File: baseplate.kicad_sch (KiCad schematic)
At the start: 8 parts, among them U1 STM32L011F4Ux, U1 TLE5009E1000FUMA1, U15 DF52-4S-0.8H(21)

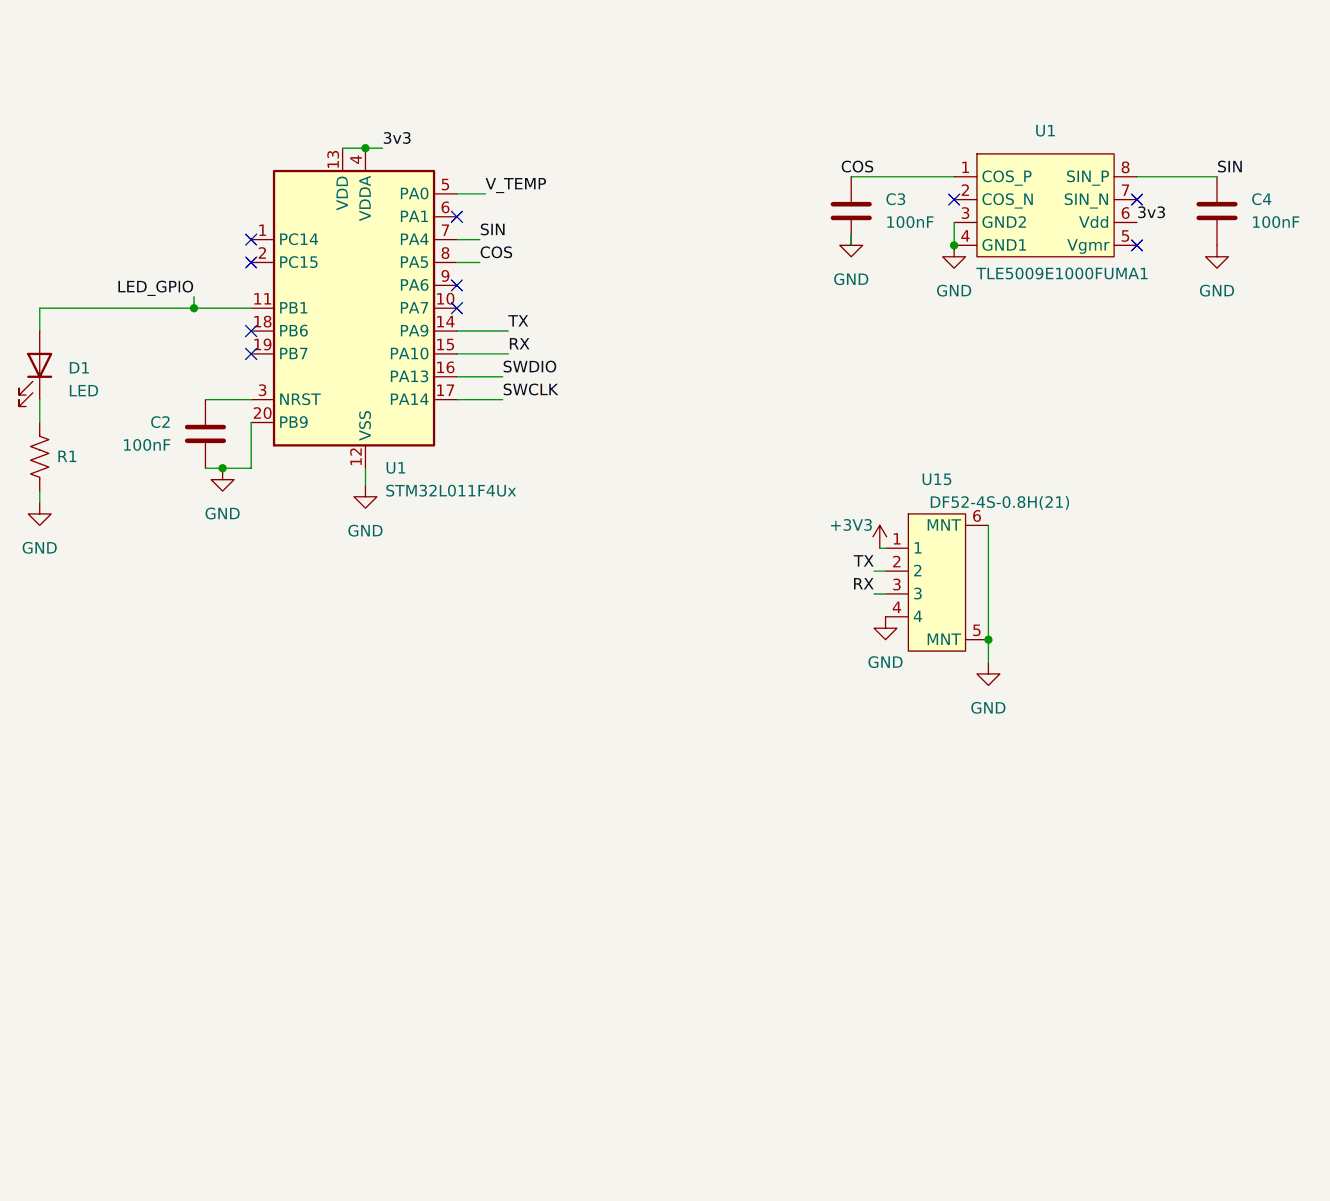
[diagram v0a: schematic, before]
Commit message: dxfs copied over, baseplate pcb fully designed, more lib management
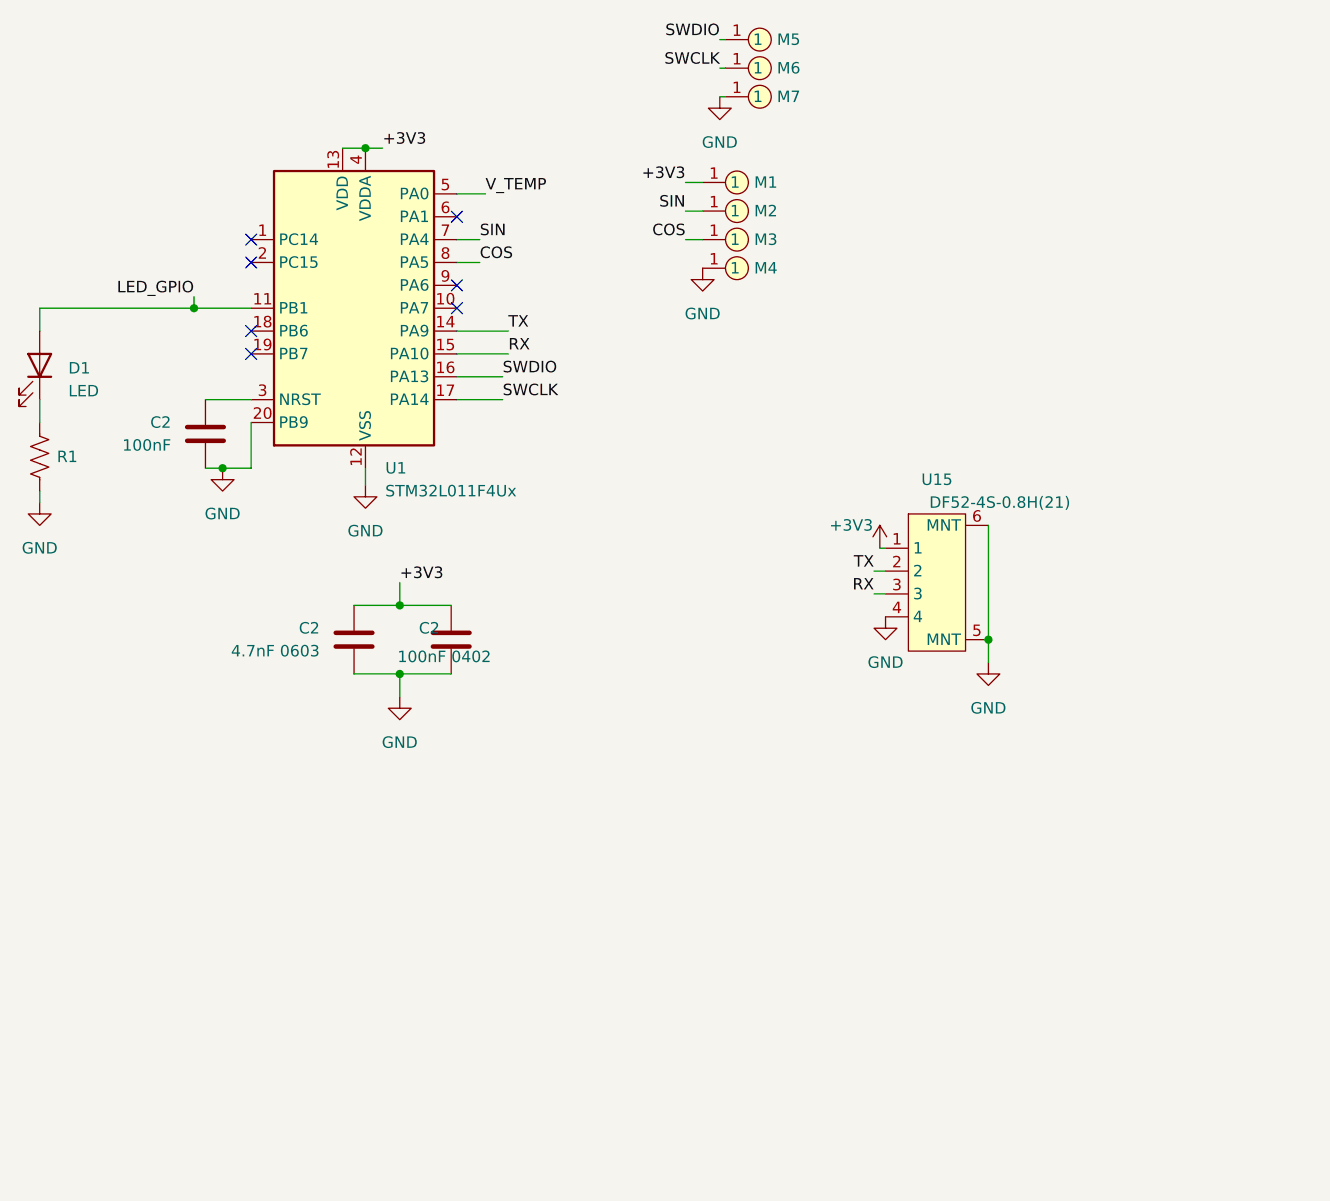
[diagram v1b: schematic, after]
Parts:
- removed C3, C4: 100nF, adapter-encoder:C_0402_1005Metric, symbol adapter-encoder:Capacitor
- removed U1: TLE5009E1000FUMA1, adapter-encoder:SOIC8-TLE5009, symbol adapter-encoder:TLE5009E1000FUMA1
- added C2: 4.7nF 0603, adapter-encoder:C_0603_1608Metric, symbol adapter-encoder:Capacitor
- added C2: 100nF 0402, adapter-encoder:C_0402_1005Metric, symbol adapter-encoder:Capacitor
- added M1, M4: THRU_HOLE_PAD, adapter-encoder:dogbone_slot, symbol adapter-encoder:THRU_HOLE_PAD
- added M2, M3: THRU_HOLE_PAD, adapter-encoder:dogbone_pad, symbol adapter-encoder:THRU_HOLE_PAD
- added M5, M6, M7: THRU_HOLE_PAD, foc-pcb-library:PAD-BREADBOARD, symbol adapter-encoder:THRU_HOLE_PAD
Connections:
- net 3v3 is gone; now on net +3V3: U1.13 (VDD), U1.4 (VDDA)
- net +3V3: now also C2.1, C2.1, M1.1
- net COS: now also M3.1
- net GND: now also C2.2, C2.2, M4.1, M7.1
- net SIN: now also M2.1
- net SWCLK: now also M6.1
- net SWDIO: now also M5.1
- no-connect marks 10 -> 7

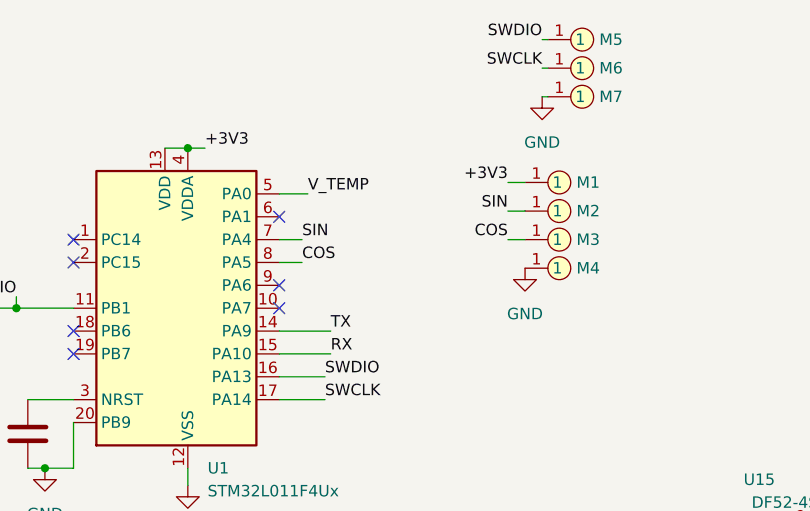
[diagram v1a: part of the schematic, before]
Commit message: net labelling, silkscreen, boards finished
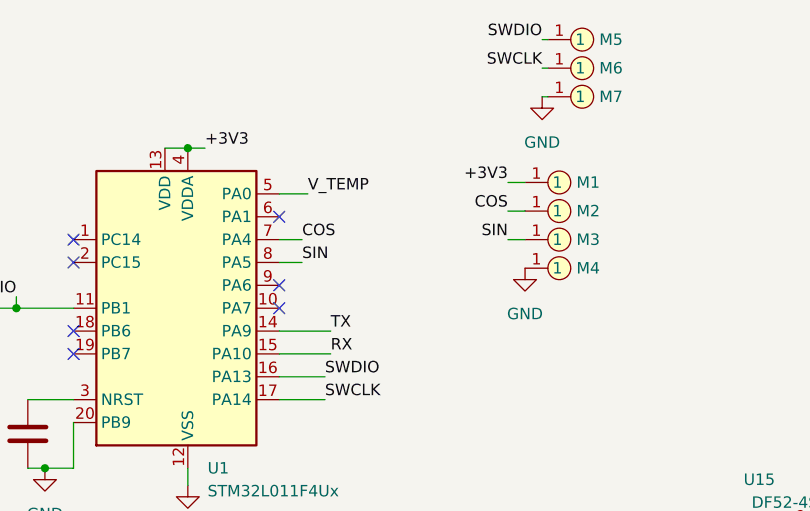
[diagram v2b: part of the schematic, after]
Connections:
- net COS: now also M2.1, U1.7 (PA4); no longer M3.1, U1.8 (PA5)
- net SIN: now also M3.1, U1.8 (PA5); no longer M2.1, U1.7 (PA4)
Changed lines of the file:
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@@
     (effects (font (size 1.27 1.27)) (justify right bottom))
   )
-  (label "COS" (at 106.68 37.465 180) (fields_autoplaced)
+  (label "SIN" (at 106.68 37.465 180) (fields_autoplaced)
     (effects (font (size 1.27 1.27)) (justify right bottom))
   )
@@
     (effects (font (size 1.27 1.27)) (justify left bottom))
   )
+  (label "COS" (at 83.82 37.465 0) (fields_autoplaced)
+    (effects (font (size 1.27 1.27)) (justify left bottom))
+  )
   (label "+3V3" (at 74.93 75.565 0) (fields_autoplaced)
     (effects (font (size 1.27 1.27)) (justify left bottom))
   )
-  (label "SIN" (at 83.82 37.465 0) (fields_autoplaced)
-    (effects (font (size 1.27 1.27)) (justify left bottom))
+  (label "COS" (at 106.68 34.29 180) (fields_autoplaced)
+    (effects (font (size 1.27 1.27)) (justify right bottom))
   )
-  (label "COS" (at 83.82 40.005 0) (fields_autoplaced)
+  (label "SIN" (at 83.82 40.005 0) (fields_autoplaced)
     (effects (font (size 1.27 1.27)) (justify left bottom))
   )
@@
     (effects (font (size 1.27 1.27)) (justify right bottom))
   )
-  (label "SIN" (at 106.68 34.29 180) (fields_autoplaced)
-    (effects (font (size 1.27 1.27)) (justify right bottom))
-  )

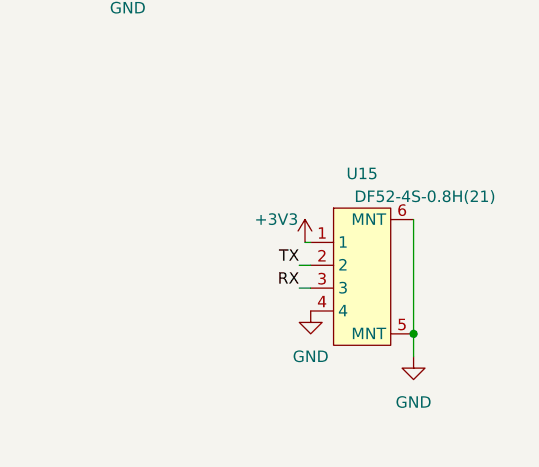
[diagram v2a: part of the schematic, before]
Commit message: step files from freecad, put the connector on the baseplate on the bottom of the baseplate
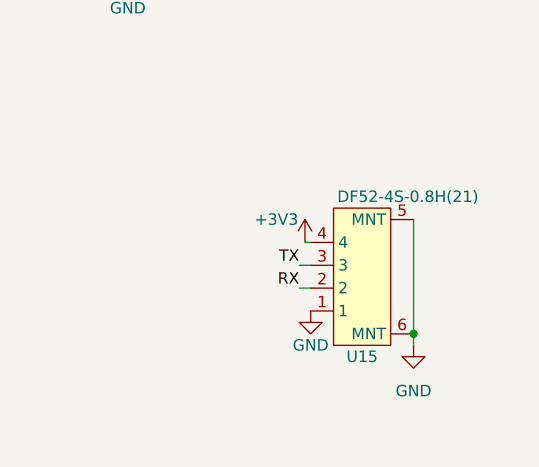
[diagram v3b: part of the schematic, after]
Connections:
- net +3V3: now also U15.4; no longer U15.1
- net GND: now also U15.1; no longer U15.4
- net RX: now also U15.2; no longer U15.3
- net TX: now also U15.3; no longer U15.2

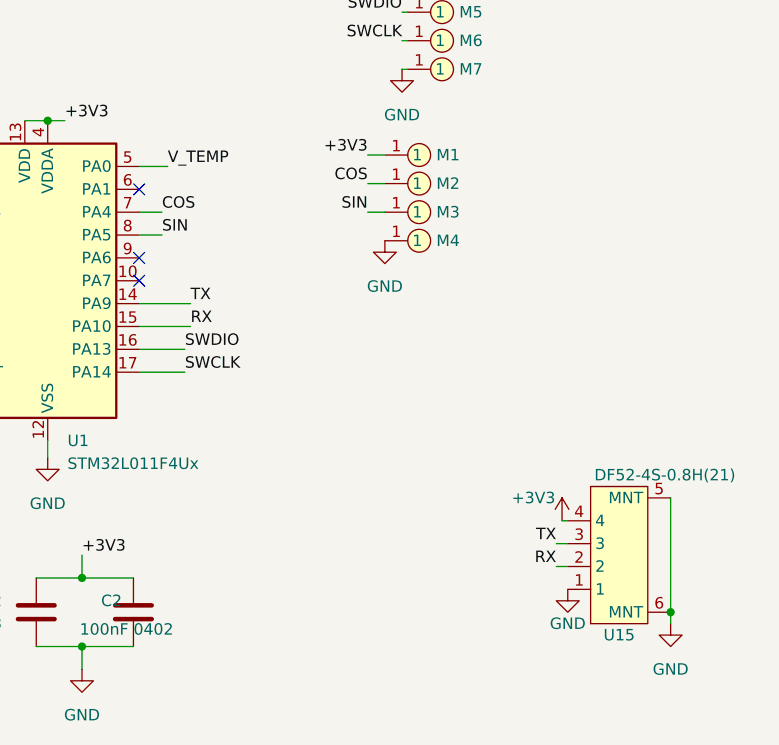
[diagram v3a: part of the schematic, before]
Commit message: reverted baseplate back to all on top, designed to flip over, and solder from the component side. dogbone bottom changed so one end has three prongs
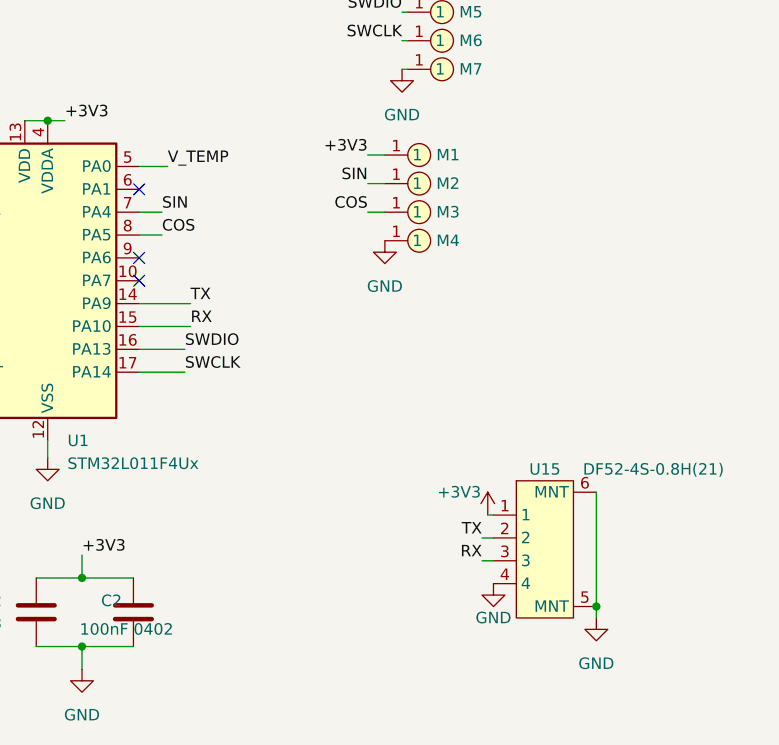
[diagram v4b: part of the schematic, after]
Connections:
- net +3V3: now also U15.1; no longer U15.4
- net COS: now also M3.1, U1.8 (PA5); no longer M2.1, U1.7 (PA4)
- net GND: now also U15.4; no longer U15.1
- net RX: now also U15.3; no longer U15.2
- net SIN: now also M2.1, U1.7 (PA4); no longer M3.1, U1.8 (PA5)
- net TX: now also U15.2; no longer U15.3
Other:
- moved on the sheet: U15

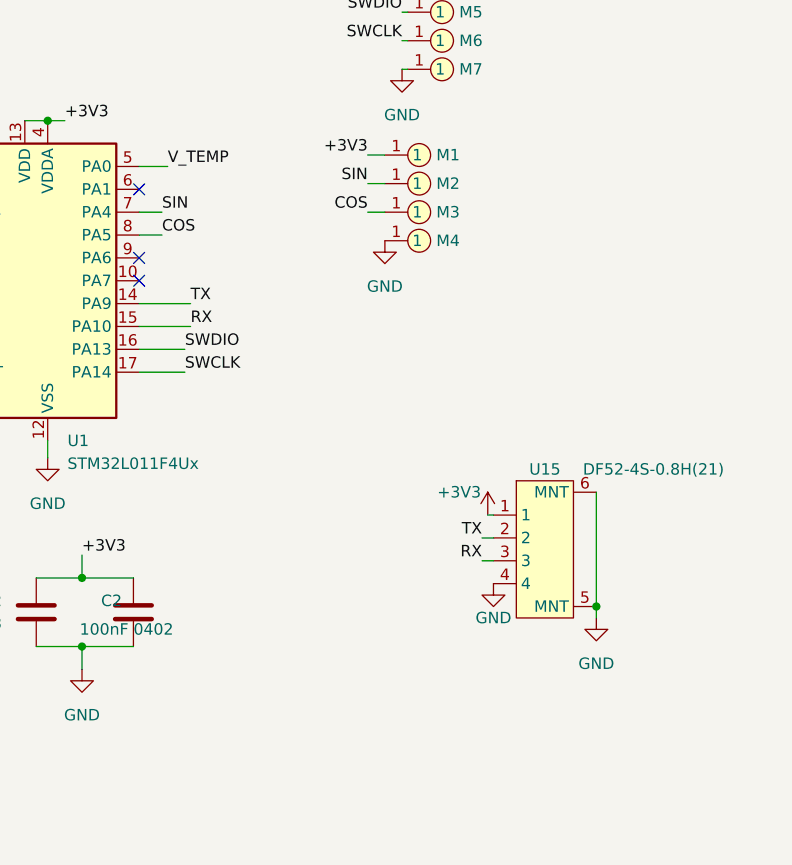
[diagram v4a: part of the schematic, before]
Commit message: updated baseplate dsign
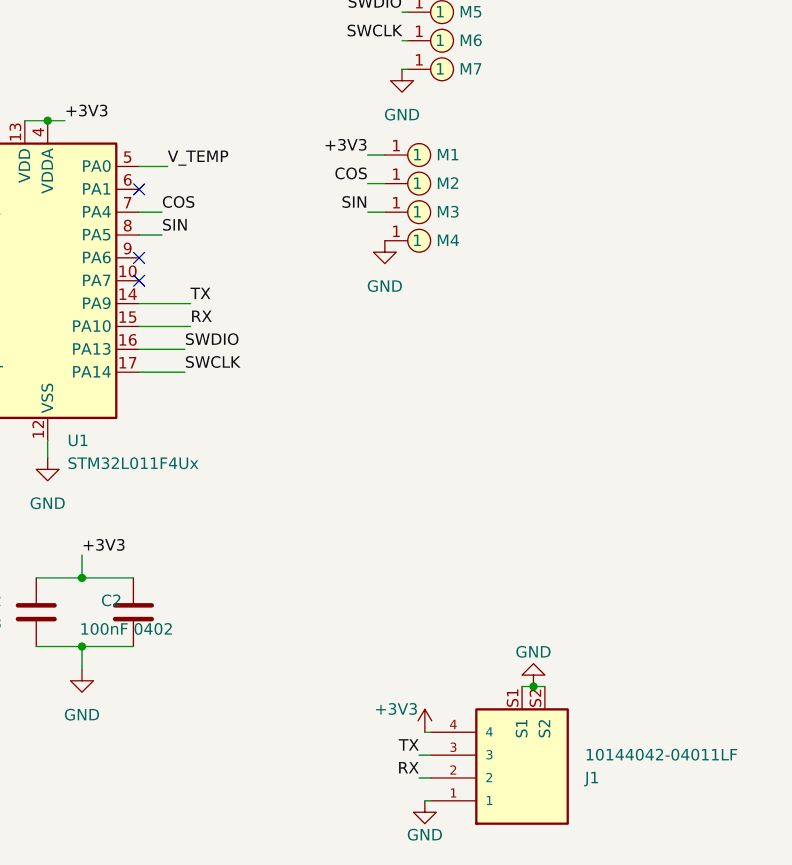
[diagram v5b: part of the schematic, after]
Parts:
- removed U15: DF52-4S-0.8H(21), foc-pcb-library:DF52-4S-0.8H(21), symbol foc-pcb:DF52-4S-0.8H(21)
- added J1: 10144042-04011LF, adapter-encoder:AMPHENOL_10144042-04011LF, symbol adapter-encoder:10144042-04011LF
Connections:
- net +3V3: now also J1.4
- net COS: now also M2.1, U1.7 (PA4); no longer M3.1, U1.8 (PA5)
- net GND: now also J1.1, J1.S1, J1.S2
- net RX: now also J1.2
- net SIN: now also M3.1, U1.8 (PA5); no longer M2.1, U1.7 (PA4)
- net TX: now also J1.3

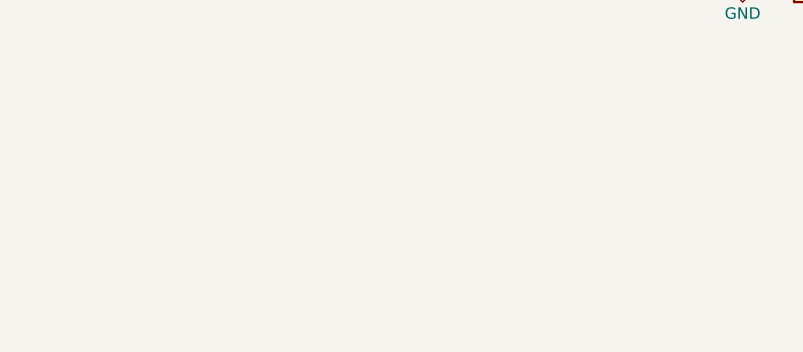
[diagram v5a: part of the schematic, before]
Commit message: mounting holes
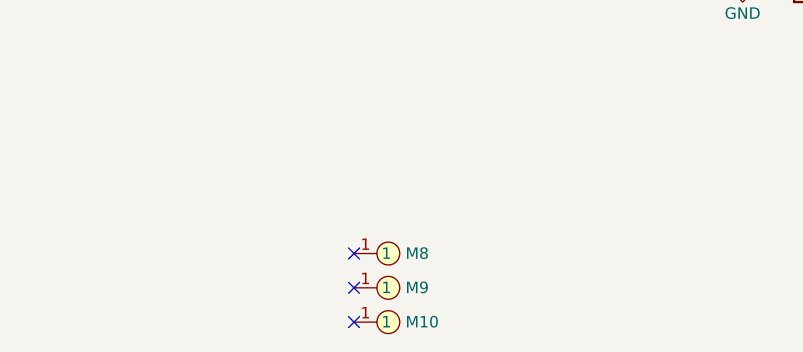
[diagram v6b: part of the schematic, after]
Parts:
- added M10, M8, M9: THRU_HOLE_PAD, adapter-encoder:MountingHole3mm, symbol adapter-encoder:THRU_HOLE_PAD
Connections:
- no-connect marks 7 -> 10
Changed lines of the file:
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@@
   )
   (no_connect (at 81.28 42.545))
+  (no_connect (at 69.85 140.97))
+  (no_connect (at 69.85 133.35))
   (no_connect (at 81.28 34.925))
   (no_connect (at 81.28 45.085))
+  (no_connect (at 69.85 137.16))
   (no_connect (at 58.42 40.005))
   (no_connect (at 58.42 37.465))
@@
         (path "/a662c0e4-ec1a-48b1-bec9-50725807a156"
           (reference "M5") (unit 1)
+        )
+      )
+    )
+  )
+  (symbol (lib_id "adapter-encoder:THRU_HOLE_PAD") (at 72.39 133.35 0) (unit 1)
+    (in_bom no) (on_board yes) (dnp no) (fields_autoplaced)
+    (property "Reference" "M8" (at 75.565 133.35 0)
+      (effects (font (size 1.27 1.27)) (justify left))
+    )
+    (property "Value" "THRU_HOLE_PAD" (at 72.39 129.54 0)
+      (effects (font (size 1.27 1.27)) hide)
+    )
+    (property "Footprint" "adapter-encoder:MountingHole3mm" (at 74.93 130.81 0)
+      (effects (font (size 1.27 1.27)) hide)
+    )
+    (property "Datasheet" "" (at 72.39 133.35 0)
+      (effects (font (size 1.27 1.27)) hide)
+    )
+    (pin "1")
+    (instances
+      (project "baseplate"
+        (path "/a662c0e4-ec1a-48b1-bec9-50725807a156"
+          (reference "M8") (unit 1)
         )
       )
@@
     )
   )
+  (symbol (lib_id "adapter-encoder:THRU_HOLE_PAD") (at 72.39 137.16 0) (unit 1)
+    (in_bom no) (on_board yes) (dnp no) (fields_autoplaced)
+    (property "Reference" "M9" (at 75.565 137.16 0)
+      (effects (font (size 1.27 1.27)) (justify left))
+    )
+    (property "Value" "THRU_HOLE_PAD" (at 72.39 133.35 0)
+      (effects (font (size 1.27 1.27)) hide)
+    )
+    (property "Footprint" "adapter-encoder:MountingHole3mm" (at 74.93 134.62 0)
+      (effects (font (size 1.27 1.27)) hide)
+    )
+    (property "Datasheet" "" (at 72.39 137.16 0)
+      (effects (font (size 1.27 1.27)) hide)
+    )
+    (pin "1")
+    (instances
+      (project "baseplate"
+        (path "/a662c0e4-ec1a-48b1-bec9-50725807a156"
+          (reference "M9") (unit 1)
+        )
+      )
+    )
+  )
   (symbol (lib_id "adapter-encoder:Capacitor") (at 80.645 81.915 0) (mirror y) (unit 1)
     (in_bom yes) (on_board yes) (dnp no)
@@
         )
       )
+    )
+  )
+  (symbol (lib_id "adapter-encoder:THRU_HOLE_PAD") (at 72.39 140.97 0) (unit 1)
+    (in_bom no) (on_board yes) (dnp no) (fields_autoplaced)
+    (property "Reference" "M10" (at 75.565 140.97 0)
+      (effects (font (size 1.27 1.27)) (justify left))
+    )
+    (property "Value" "THRU_HOLE_PAD" (at 72.39 137.16 0)
+      (effects (font (size 1.27 1.27)) hide)
+    )
+    (property "Footprint" "adapter-encoder:MountingHole3mm" (at 74.93 138.43 0)
+      (effects (font (size 1.27 1.27)) hide)
+    )
+    (property "Datasheet" "" (at 72.39 140.97 0)
+      (effects (font (size 1.27 1.27)) hide)
+    )
+    (pin "1")
+    (instances
+      (project "baseplate"
+        (path "/a662c0e4-ec1a-48b1-bec9-50725807a156"
+          (reference "M10") (unit 1)
+        )
+      )
